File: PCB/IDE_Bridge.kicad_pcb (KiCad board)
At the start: 2 copper layers, 48 x 52 mm, 93 parts, among them J1 IDE Connector, P1 USB_C_Plug_USB2.0, SW1 BOOTSEL, U1 74HCT245, U2 74HCT125, U3 74HCT125, U4 74HCT245, U5 RP2354B, U6 TVS, U7 LDO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

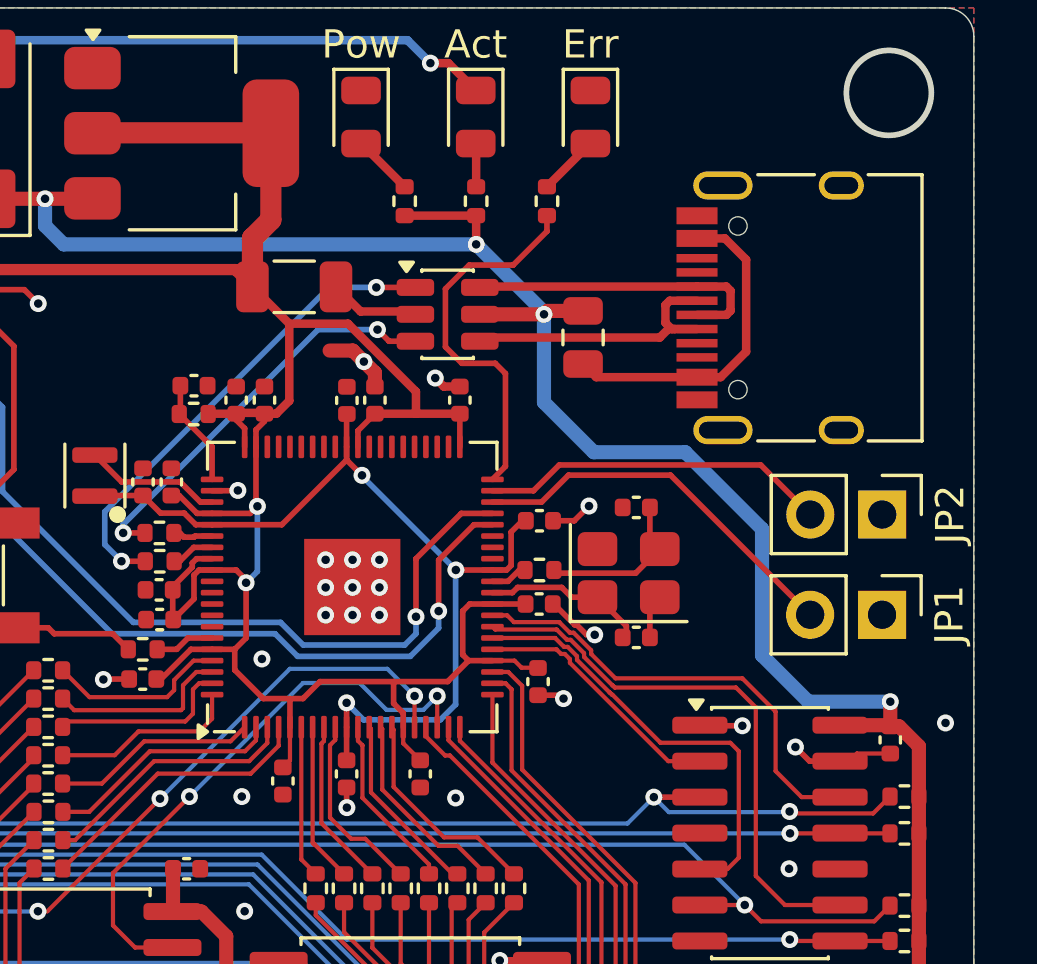
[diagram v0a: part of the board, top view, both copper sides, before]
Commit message: Updated PCB
Rev .6 of PCB:  FIxed USB-C connector position, and added 5.1k pulldowns for CC1/CC2
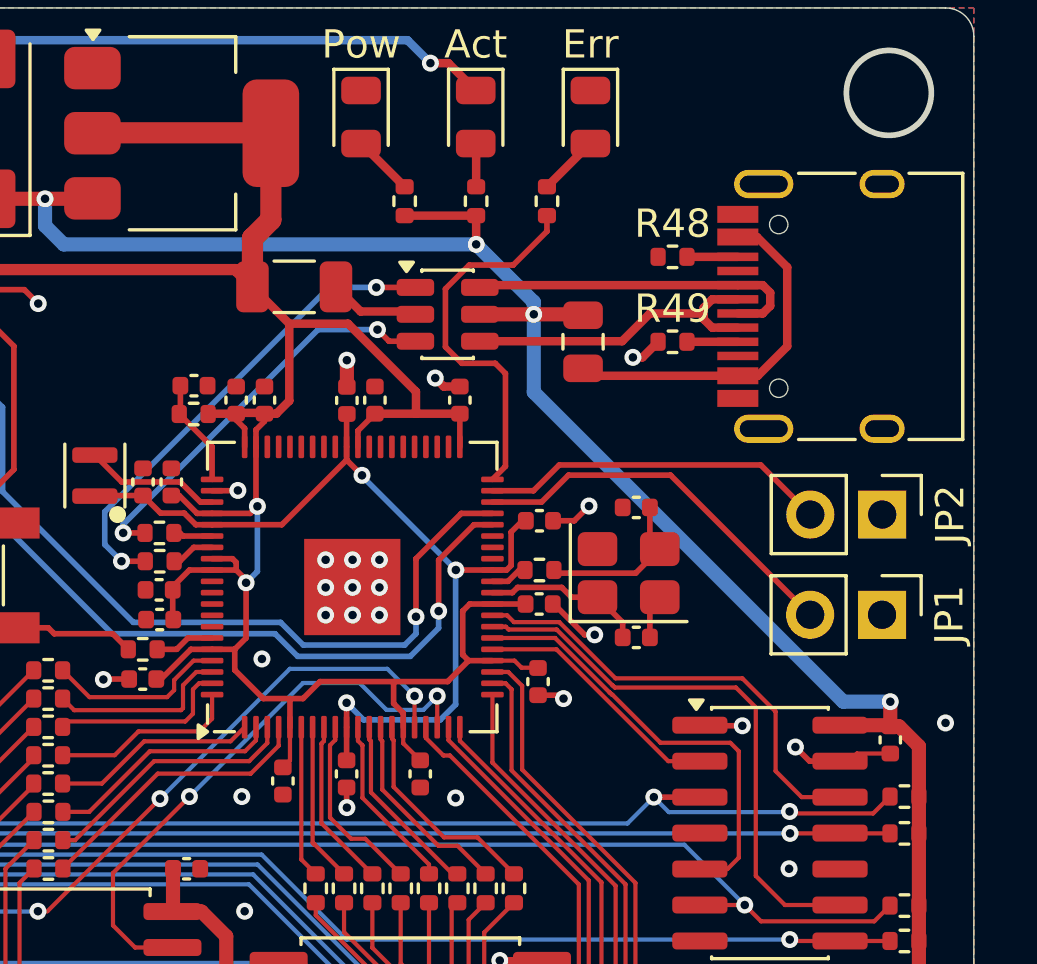
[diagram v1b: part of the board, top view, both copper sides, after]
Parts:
- added R48: 5.1k, Resistor_SMD:R_0402_1005Metric, F.Cu at (155.9, 84.3)
- added R49: 5.1k, Resistor_SMD:R_0402_1005Metric, F.Cu at (155.9, 87.3)
- moved P1 1.44 mm to (162.2, 86.0)
- moved F1 0.15 mm to (152.7, 87.3)
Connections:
- P1 pad A5: unconnected-(P1-CC-PadA5) -> Net-(P1-CC)
- P1 pad B5: unconnected-(P1-VCONN-PadB5) -> Net-(P1-VCONN)
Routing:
- net +5V: track 177.6 -> 175.0 mm
- net Net-(P1-VCONN): track 0.00 -> 1.79 mm
- net Net-(P1-CC): track 0.00 -> 1.79 mm
- net +3.3V: track 90.5 -> 88.8 mm
- net Net-(P1-D--PadA7): track 10.1 -> 11.4 mm
- net Net-(F1-Pad2): track 11.6 -> 12.9 mm
- net Net-(P1-D+-PadA6): track 10.9 -> 12.1 mm
- net GND: track 36.9 -> 36.6 mm, vias 36 -> 37
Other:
- board text added: "ATAboy Rev 0.6 JJ Dasher © 2026"
- board text removed: "ATAboy Rev 0.5 JJ Dasher © 2026"
